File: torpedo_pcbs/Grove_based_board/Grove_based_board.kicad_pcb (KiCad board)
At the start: 2 copper layers, 75 x 27.5 mm, 1 part

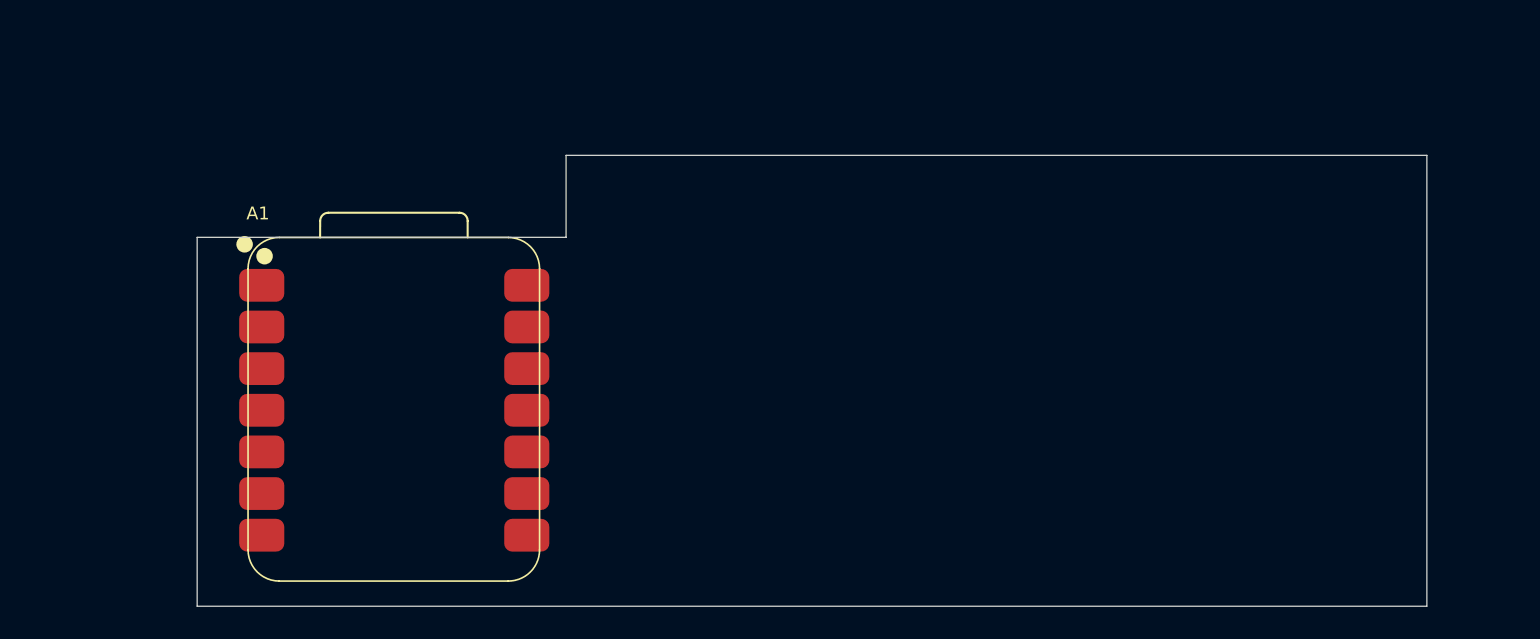
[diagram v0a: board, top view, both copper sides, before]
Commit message: sensors pcb and main pcb improvements
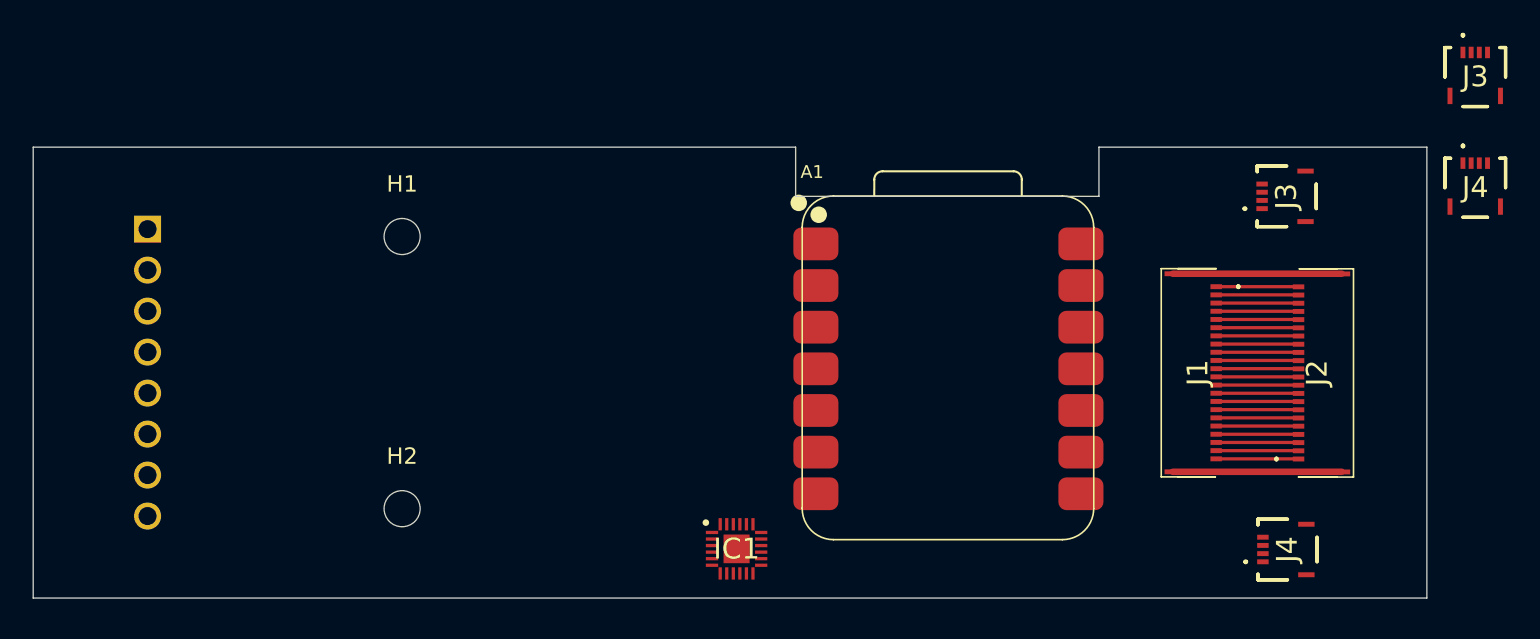
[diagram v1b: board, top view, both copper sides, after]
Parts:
- added H1: MountingHole, MountingHole:MountingHole_2.2mm_M2, F.Cu at (122.5, 87.5)
- added H2: MountingHole, MountingHole:MountingHole_2.2mm_M2, F.Cu at (122.5, 104.0)
- added IC1: ICM-20948, SamacSys_Parts:QFN40P300X300X105-25N-D, F.Cu at (142.9, 106.5)
- added J1: 503480-2200, SamacSys_Parts:5034802200, F.Cu at (172.4, 95.8)
- added J2: 503480-2200, SamacSys_Parts:5034802200, F.Cu at (176.9, 95.8)
- added J3: 503480-0440, SamacSys_Parts:5034800440, F.Cu at (176.4, 85.0)
- added J3: 503480-0440, SamacSys_Parts:5034800440, F.Cu at (187.9, 77.7)
- added J4: 503480-0440, SamacSys_Parts:5034800440, F.Cu at (187.9, 84.5)
- added J4: 503480-0440, SamacSys_Parts:5034800440, F.Cu at (176.5, 106.5)
- added J5: S8B-EH, SamacSys_Parts:SHDRRA8W64P0X250_1X8_2250X820X420P, B.Cu at (107.0, 87.0)
- moved A1 33.9 mm to (155.8, 95.5)
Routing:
- net GND: track 0.00 -> 20.7 mm
- net Net-(J1-Pad1): track 0.00 -> 5.03 mm
- net Net-(J1-Pad9): track 0.00 -> 5.02 mm
- net Net-(J1-Pad8): track 0.00 -> 5.02 mm
- net Net-(J1-Pad7): track 0.00 -> 5.02 mm
- net Net-(J1-Pad6): track 0.00 -> 5.02 mm
- net Net-(J1-Pad5): track 0.00 -> 5.02 mm
- net Net-(J1-Pad4): track 0.00 -> 5.02 mm
- net Net-(J1-Pad3): track 0.00 -> 5.02 mm
- net Net-(J1-Pad22): track 0.00 -> 5.02 mm
- net Net-(J1-Pad21): track 0.00 -> 5.02 mm
- net Net-(J1-Pad20): track 0.00 -> 5.02 mm
- net Net-(J1-Pad2): track 0.00 -> 5.02 mm
- net Net-(J1-Pad19): track 0.00 -> 5.02 mm
- net Net-(J1-Pad18): track 0.00 -> 5.02 mm
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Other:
- board size 75 x 27.5 mm -> 85 x 27.5 mm

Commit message: save feb21
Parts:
- removed A1: XIAO ESP32S3, board_board_connection:XIAO ESP32S3 SMD
- removed H1, H2: MountingHole, MountingHole:MountingHole_2.2mm_M2
- removed J1, J2: 503480-2200, SamacSys_Parts:5034802200
- removed the J3 at (176.4, 85.0)
- removed the J3 at (187.9, 77.7)
- removed the J4 at (187.9, 84.5)
- removed the J4 at (176.5, 106.5)
- removed J5: S8B-EH, SamacSys_Parts:SHDRRA8W64P0X250_1X8_2250X820X420P
- added J3: 503480-0440, SamacSys_Parts:5034800440, F.Cu at (176.6, 85.0)
- added J4: 503480-0440, SamacSys_Parts:5034800440, F.Cu at (176.5, 106.5)
- moved IC1 11.3 mm to (142.8, 95.2), turned to 180 degrees
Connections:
- IC1 pad 10: unconnected-(IC1-REGOUT-Pad10) -> Net-(IC1-REGOUT)
- IC1 pad 11: unconnected-(IC1-FSYNC-Pad11) -> GND
- IC1 pad 12: unconnected-(IC1-INT1-Pad12) -> IMU_INT
- IC1 pad 13: unconnected-(IC1-VDD-Pad13) -> +3.3V
- IC1 pad 18: unconnected-(IC1-GND-Pad18) -> GND
- IC1 pad 20: unconnected-(IC1-RESV_2-Pad20) -> GND
- IC1 pad 22: unconnected-(IC1-NCS-Pad22) -> +3.3V
- IC1 pad 23: unconnected-(IC1-SCL_/_SCLK-Pad23) -> SCL2
- IC1 pad 24: unconnected-(IC1-SDA_/_SDI-Pad24) -> SDA2
- IC1 pad 8: unconnected-(IC1-VDDIO-Pad8) -> +1V8
- IC1 pad 9: unconnected-(IC1-SDO_/_AD0-Pad9) -> GND
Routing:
- net GND: track 20.7 -> 0.00 mm
- net Net-(J1-Pad1): track 5.03 -> 0.00 mm
- net Net-(J1-Pad9): track 5.02 -> 0.00 mm
- net Net-(J1-Pad8): track 5.02 -> 0.00 mm
- net Net-(J1-Pad7): track 5.02 -> 0.00 mm
- net Net-(J1-Pad6): track 5.02 -> 0.00 mm
- net Net-(J1-Pad5): track 5.02 -> 0.00 mm
- net Net-(J1-Pad4): track 5.02 -> 0.00 mm
- net Net-(J1-Pad3): track 5.02 -> 0.00 mm
- net Net-(J1-Pad22): track 5.02 -> 0.00 mm
- net Net-(J1-Pad21): track 5.02 -> 0.00 mm
- net Net-(J1-Pad20): track 5.02 -> 0.00 mm
- net Net-(J1-Pad2): track 5.02 -> 0.00 mm
- net Net-(J1-Pad19): track 5.02 -> 0.00 mm
- net Net-(J1-Pad18): track 5.02 -> 0.00 mm
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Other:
- outline, holes or cut-outs redrawn
- copper layers 2 -> 4

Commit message: feb23 updates
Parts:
- removed IC1: ICM-20948, SamacSys_Parts:QFN40P300X300X105-25N-D
- added A1: XIAO ESP32S3, board_board_connection:XIAO ESP32S3 SMD, F.Cu at (156.8, 95.1)
- added A2: Grove AI Vision Module V2, board_board_connection:Grove conn, F.Cu at (114.5, 95.5)
- added C1: 0.1μF, Capacitor_SMD:C_0603_1608Metric, F.Cu at (66.5, 120.1)
- added C10: 1μF, Capacitor_SMD:C_0603_1608Metric, F.Cu at (45.7, 93.0)
- added C11: 2.2μF, Capacitor_SMD:C_0603_1608Metric, F.Cu at (45.7, 95.6)
- added C12: 0.1μF, Capacitor_SMD:C_0603_1608Metric, F.Cu at (45.7, 98.1)
- added C13: 10μF, Capacitor_SMD:C_0603_1608Metric, F.Cu at (45.7, 100.6)
- added C14: 0.1μF, Capacitor_SMD:C_0603_1608Metric, F.Cu at (45.7, 103.1)
- added C15: 0.1μF, Capacitor_SMD:C_0603_1608Metric, F.Cu at (45.7, 105.6)
- added C16: 0.1μF, Capacitor_SMD:C_0603_1608Metric, F.Cu at (49.7, 90.5)
- added C17: 0.1μF, Capacitor_SMD:C_0603_1608Metric, F.Cu at (49.7, 93.0)
- added C18: 1μF, Capacitor_SMD:C_0603_1608Metric, F.Cu at (49.7, 95.6)
- added C19: 10nF, Capacitor_SMD:C_0603_1608Metric, F.Cu at (49.7, 98.1)
- added C2: 0.1μF, Capacitor_SMD:C_0603_1608Metric, F.Cu at (77.3, 121.0)
- added C20: 1μF, Capacitor_SMD:C_0603_1608Metric, F.Cu at (49.7, 100.6)
- added C21: 0.1μF, Capacitor_SMD:C_0603_1608Metric, F.Cu at (49.7, 103.1)
- added C22: 10μF, Capacitor_SMD:C_0603_1608Metric, F.Cu at (202.1, 94.6)
- added C22: 10μF, Capacitor_SMD:C_0603_1608Metric, F.Cu at (49.7, 105.6)
- added C23: 10μF, Capacitor_SMD:C_0603_1608Metric, F.Cu at (202.1, 97.1)
- added C23: 10μF, Capacitor_SMD:C_0603_1608Metric, F.Cu at (53.7, 90.5)
- added C24: ??μF, Capacitor_SMD:C_0603_1608Metric, F.Cu at (53.7, 93.0)
- added C25: 1μF, Capacitor_SMD:C_0603_1608Metric, F.Cu at (53.7, 95.6)
- added C26: ??μF, Capacitor_SMD:C_0603_1608Metric, F.Cu at (53.7, 98.1)
- added C27: 0.1μF, Capacitor_SMD:C_0603_1608Metric, F.Cu at (53.7, 100.6)
- added C28: 22nF, Capacitor_SMD:C_0603_1608Metric, F.Cu at (53.7, 103.1)
- added C29: 22nF, Capacitor_SMD:C_0603_1608Metric, F.Cu at (53.7, 105.6)
- added C3: 0.1μF, Capacitor_SMD:C_0603_1608Metric, F.Cu at (45.7, 120.1)
- added C4: 0.1μF, Capacitor_SMD:C_0603_1608Metric, F.Cu at (56.1, 120.1)
- added C5: 0.1μF, Capacitor_SMD:C_0603_1608Metric, F.Cu at (45.7, 90.5)
- added C6: 47μF, Capacitor_SMD:C_0603_1608Metric, F.Cu at (66.5, 122.6)
- added C7: 47μF, Capacitor_SMD:C_0603_1608Metric, B.Cu at (83.0, 124.7)
- added C8: 47μF, Capacitor_SMD:C_0603_1608Metric, F.Cu at (45.7, 122.6)
- added C9: 47μF, Capacitor_SMD:C_0603_1608Metric, F.Cu at (56.1, 122.6)
- added D1: LED, Capacitor_SMD:C_0603_1608Metric, F.Cu at (57.7, 90.5)
- added D1: LED, Capacitor_SMD:C_0603_1608Metric, F.Cu at (202.1, 99.6)
- added D2: LED, Capacitor_SMD:C_0603_1608Metric, F.Cu at (57.7, 93.0)
- added D3: LED, Capacitor_SMD:C_0603_1608Metric, F.Cu at (57.7, 95.6)
- added D4: LED, Capacitor_SMD:C_0603_1608Metric, F.Cu at (57.7, 98.1)
- added F1: Fuse, Capacitor_SMD:C_0603_1608Metric, F.Cu at (57.7, 100.6)
- added FB1: FerriteBead, Capacitor_SMD:C_0603_1608Metric, F.Cu at (57.7, 103.1)
- added H1: MountingHole, MountingHole:MountingHole_2.2mm_M2, F.Cu at (182.0, 82.1)
- added H2: MountingHole, MountingHole:MountingHole_2.2mm_M2, F.Cu at (182.0, 108.9)
- added H3: 22pin->15pin Adapter Slot, MountingEquipment:slot, F.Cu at (168.8, 95.5)
- added IC10: LIS2MDLTR: Magnetometer, SamacSys_Parts:LGA-12, F.Cu at (202.2, 102.5)
- added IC2: DRV8213DSGR, SamacSys_Parts:SON50P200X200X80-9N, F.Cu at (108.0, 88.0)
- added IC3: DRV8213DSGR, SamacSys_Parts:SON50P200X200X80-9N, F.Cu at (108.0, 92.8)
- added IC4: DRV8213DSGR, SamacSys_Parts:SON50P200X200X80-9N, F.Cu at (108.0, 98.0)
- added IC5: DRV8213DSGR, SamacSys_Parts:SON50P200X200X80-9N, F.Cu at (108.0, 103.0)
- added IC6: VEML6040A3OG, SamacSys_Parts:VEML6040A3OG, F.Cu at (68.4, 114.6)
- added IC7: AP7362-33SP-13, SamacSys_Parts:SOIC127P600X150-9N, F.Cu at (47.9, 110.1)
- added IC7: AP7362-33SP-13: Batt->3.3V, SamacSys_Parts:SOIC127P600X150-9N, F.Cu at (204.4, 90.1)
- added IC8: TPS76918DBVR, SamacSys_Parts:SOT95P280X145-5N, F.Cu at (75.7, 113.0)
- added IC8: TPS76918DBVR: 3.3V->1.8V, SamacSys_Parts:SOT95P280X145-5N, F.Cu at (206.8, 95.7)
- added IC9: TPS60150DRVR: 3.3V->5V, SamacSys_Parts:SON65P200X200X80-7N, F.Cu at (206.3, 104.3)
- added J1: 503480-2200, SamacSys_Parts:5034802200, B.Cu at (178.1, 95.5)
- added J10: UART Comms, Connector_PinSocket_2.00mm:PinSocket_2x02_P2.00mm_Vertical, F.Cu at (77.1, 100.6)
- added J11: LCD Screen, Connector_PinSocket_2.00mm:PinSocket_2x02_P2.00mm_Vertical, F.Cu at (77.1, 106.7)
- added J12: Conn_01x01, Connector_PinHeader_1.27mm:PinHeader_1x01_P1.27mm_Vertical, F.Cu at (45.8, 115.0)
- added J13: Fan, Connector_PinSocket_1.27mm:PinSocket_1x02_P1.27mm_Vertical, F.Cu at (59.3, 108.5)
- added J2: 503480-2200, SamacSys_Parts:5034802200, B.Cu at (177.0, 95.5)
- added J5: Push-in Terminals, SamacSys_Parts:009276008021106, F.Cu at (100.8, 95.5)
- added J6: LiHV (3.8V), Connector_PinHeader_2.54mm:PinHeader_1x02_P2.54mm_Vertical, F.Cu at (110.8, 95.5)
- added Q1: BSS138, Package_TO_SOT_SMD:SOT-23, F.Cu at (54.6, 109.2)
- added Q2: BSS138, Package_TO_SOT_SMD:SOT-23, F.Cu at (54.6, 113.9)
- added R1: 8.45k, Resistor_SMD:R_0805_2012Metric, F.Cu at (70.7, 120.3)
- added R10: R, Resistor_SMD:R_0201_0603Metric, F.Cu at (88.0, 82.9)
- added R11: R, Resistor_SMD:R_0201_0603Metric, F.Cu at (88.0, 84.6)
- added R12: 10k, Resistor_SMD:R_0201_0603Metric, F.Cu at (88.0, 86.4)
- added R13: 20k, Resistor_SMD:R_0201_0603Metric, F.Cu at (88.0, 88.1)
- added R14: 10k, Resistor_SMD:R_0201_0603Metric, F.Cu at (88.0, 89.9)
- added R15: 10k, Resistor_SMD:R_0201_0603Metric, F.Cu at (90.4, 82.9)
- added R16: 10k, Resistor_SMD:R_0201_0603Metric, F.Cu at (90.4, 84.6)
- added R17: 10k, Resistor_SMD:R_0201_0603Metric, F.Cu at (90.4, 86.4)
- added R18: ???, Resistor_SMD:R_0201_0603Metric, F.Cu at (90.4, 88.1)
- added R2: 8.45k, Resistor_SMD:R_0805_2012Metric, F.Cu at (82.0, 120.1)
- added R3: 8.45k, Resistor_SMD:R_0805_2012Metric, F.Cu at (49.9, 120.3)
- added R4: 8.45k, Resistor_SMD:R_0805_2012Metric, F.Cu at (60.3, 120.3)
- added R5: 10k, Resistor_SMD:R_0201_0603Metric, F.Cu at (85.5, 82.9)
- added R6: R, Resistor_SMD:R_0201_0603Metric, F.Cu at (201.4, 105.0)
- added R6: R, Resistor_SMD:R_0201_0603Metric, F.Cu at (85.5, 84.6)
- added R7: 2.2k, Resistor_SMD:R_0201_0603Metric, F.Cu at (85.5, 86.4)
- added R8: 2.2k, Resistor_SMD:R_0201_0603Metric, F.Cu at (85.5, 88.1)
- added R9: R, Resistor_SMD:R_0201_0603Metric, F.Cu at (85.5, 89.9)
- added SW1: SW_SPDT, Connector_PinSocket_1.27mm:PinSocket_1x02_P1.27mm_Vertical, F.Cu at (59.3, 113.1)
- added U1: STLINK-V3MINIE Edge Connector, edge connector:STLINK-V3MINIE conn, F.Cu at (85.1, 78.0)
- added U2: STM32G473CBU6, Package_DFN_QFN:QFN-48-1EP_7x7mm_P0.5mm_EP5.6x5.6mm, F.Cu at (126.1, 95.5)
- added U3: LSM6DSOTR: Acc+Gyro+Temp, SamacSys_Parts:LGA-14L_2P5X3X0P86_STM, F.Cu at (206.5, 100.1)
- added U4: ILPS22QS: Air Pressure+Temp, SamacSys_Parts:LPS22HHTR, F.Cu at (210.4, 104.2)
- moved J4 0.27 mm to (176.6, 106.3)
- moved J3 0.25 mm to (176.6, 84.7)
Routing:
- net /Motor driver0/OUT1: track 0.00 -> 7.70 mm
- net /Motor driver3/OUT2: track 0.00 -> 7.10 mm
- net /Motor driver3/OUT1: track 0.00 -> 7.10 mm
- net /Motor driver2/OUT2: track 0.00 -> 7.10 mm
- net /Motor driver1/OUT1: track 0.00 -> 7.10 mm
- net /Motor driver0/OUT2: track 0.00 -> 7.10 mm
- net /Motor driver2/OUT1: track 0.00 -> 7.10 mm
- net /Motor driver1/OUT2: track 0.00 -> 7.10 mm
- net MOTOR1_IPROPI: track 0.00 -> 3.56 mm
- net Net-(J1-Pad14): track 0.00 -> 1.60 mm
- net Net-(J1-Pad20): track 0.00 -> 1.60 mm
- net Net-(J1-Pad7): track 0.00 -> 1.60 mm
- net Net-(J1-Pad19): track 0.00 -> 1.60 mm
- net Net-(J1-Pad16): track 0.00 -> 1.60 mm
- net Net-(J1-Pad10): track 0.00 -> 1.60 mm
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- added copper zone on In2.Cu, net +3.3V
- added copper zone on In2.Cu, net +BATT
- added copper zone on In1.Cu, net GND
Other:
- board size 85 x 27.5 mm -> 89 x 31 mm

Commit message: flex_pcb_updates
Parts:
- added J9: MTF-02P Connector, Connector_PinSocket_2.00mm:PinSocket_2x02_P2.00mm_Vertical, F.Cu at (105.2, 123.8)
- F1: value Fuse -> Fuse Holder
- IC10: moved to B.Cu
- moved IC6 78.8 mm to (139.9, 81.6)
- moved U3 63.9 mm to (142.8, 95.5), turned to 90 degrees
- moved IC10 52.2 mm to (150.4, 109.2), turned to 180 degrees
- moved U4 25.0 mm to (192.5, 86.8)
- moved U2 1.77 mm to (127.9, 95.3)
